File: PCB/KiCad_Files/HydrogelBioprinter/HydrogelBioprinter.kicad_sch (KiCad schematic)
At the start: 24 parts, among them J1 USB_B_Micro, J2 Conn_01x04_Pin, SW1 SW_Push, SW2 SW_SPDT, U1 STM32F407VGT6, Y1 16MHz

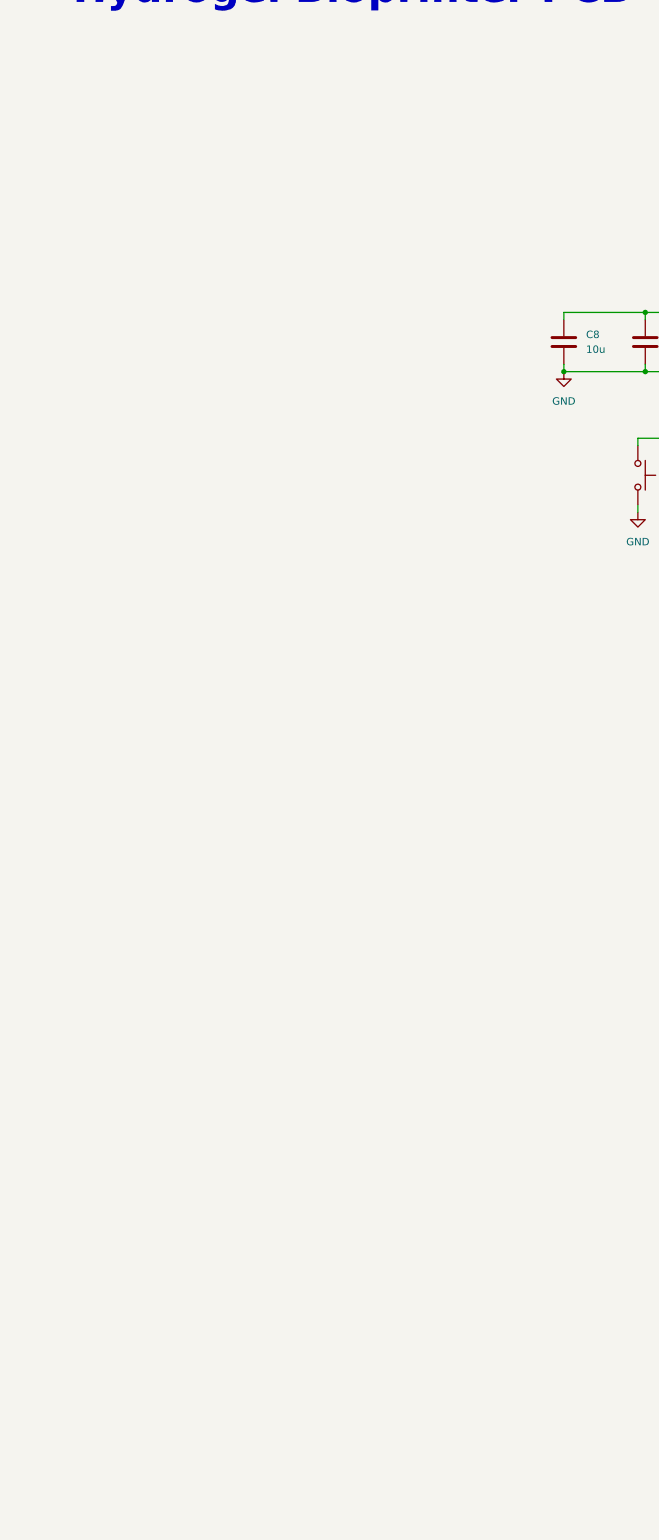
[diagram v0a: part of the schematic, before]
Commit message: Added driver connections to PCB KiCad Schematic
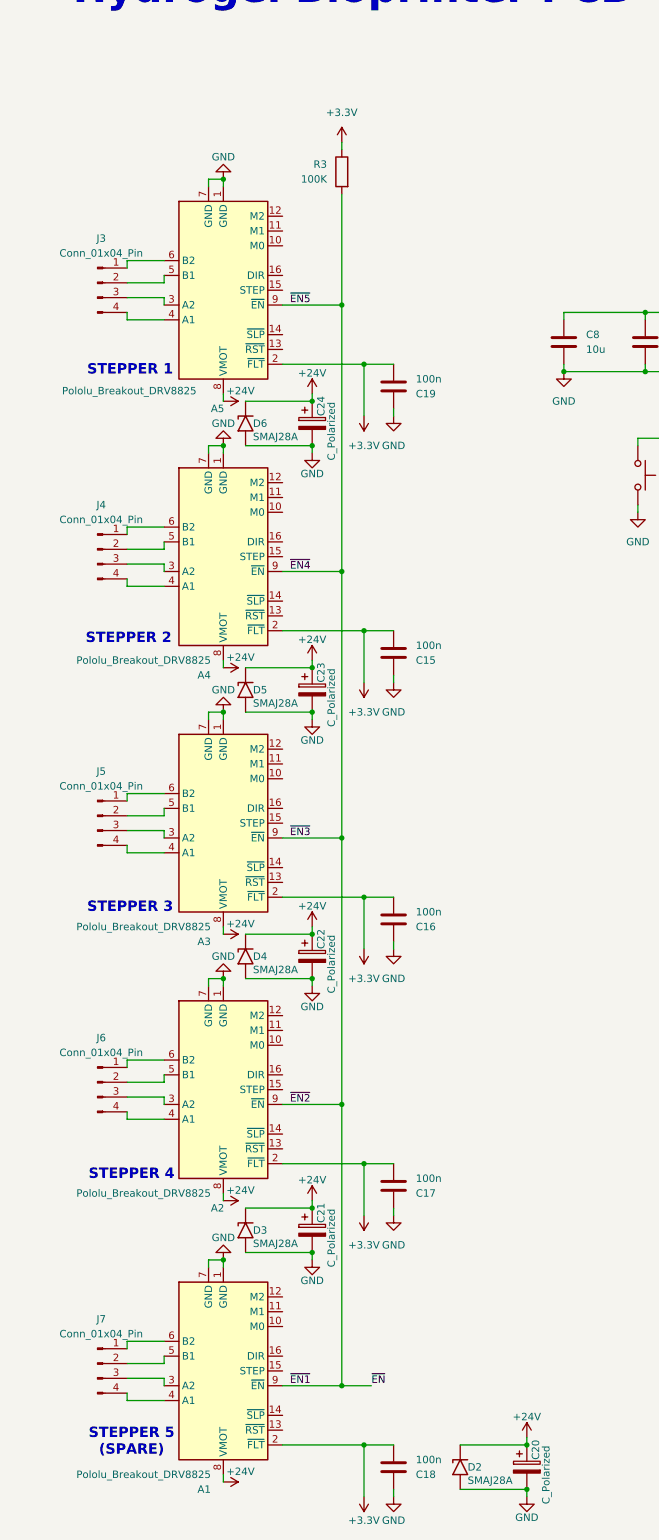
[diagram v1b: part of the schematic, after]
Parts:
- added A1, A2, A3, A4, A5: Pololu_Breakout_DRV8825, Module:Pololu_Breakout-16_15.2x20.3mm, symbol Driver_Motor:Pololu_Breakout_DRV8825
- added C15, C16, C17, C18, C19: 100n, symbol Device:C
- added C20, C21, C22, C23, C24: C_Polarized, Capacitor_SMD:CP_Elec_6.3x7.7, symbol Device:C_Polarized
- added D2, D3, D4, D5, D6: SMAJ28A, Diode_SMD:D_SMA, symbol Diode:SMAJ28A
- added J3, J4, J5, J6, J7: Conn_01x04_Pin, symbol Connector:Conn_01x04_Pin
- added R3: 100K, symbol Device:R
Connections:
- net +3.3V: now also A1.2 (~{FLT}), A2.2 (~{FLT}), A3.2 (~{FLT}), A4.2 (~{FLT}), A5.2 (~{FLT}), C15.2, C16.2, C17.2, C18.2, C19.2, R3.1
- net GND: now also A1.1 (GND), A1.7 (GND), A2.1 (GND), A2.7 (GND), A3.1 (GND), A3.7 (GND), A4.1 (GND), A4.7 (GND), A5.1 (GND), A5.7 (GND), C15.1, C16.1, C17.1, C18.1, C19.1, C20.2, C21.2, C22.2, C23.2, C24.2, D2.2 (A2), D3.2 (A2), D4.2 (A2), D5.2 (A2), D6.2 (A2)
- new net: A1.3 (A2), J7.3 (Pin_3)
- new net: A1.4 (A1), J7.4 (Pin_4)
- new net: A1.5 (B1), J7.2 (Pin_2)
- new net: A1.6 (B2), J7.1 (Pin_1)
- new net: A4.6 (B2), J4.1 (Pin_1)
- new net: A4.5 (B1), J4.2 (Pin_2)
- new net: A4.3 (A2), J4.3 (Pin_3)
- new net: A4.4 (A1), J4.4 (Pin_4)
- new net: A5.3 (A2), J3.3 (Pin_3)
- new net: A5.4 (A1), J3.4 (Pin_4)
- new net: A5.5 (B1), J3.2 (Pin_2)
- new net: A5.6 (B2), J3.1 (Pin_1)
- new net: A3.6 (B2), J5.1 (Pin_1)
- new net: A3.5 (B1), J5.2 (Pin_2)
- new net: A3.3 (A2), J5.3 (Pin_3)
- new net: A3.4 (A1), J5.4 (Pin_4)
- new net: A2.3 (A2), J6.3 (Pin_3)
- new net: A2.4 (A1), J6.4 (Pin_4)
- new net: A2.5 (B1), J6.2 (Pin_2)
- new net: A2.6 (B2), J6.1 (Pin_1)
- new net +24V: A1.8 (VMOT), A2.8 (VMOT), A3.8 (VMOT), A4.8 (VMOT), A5.8 (VMOT), C20.1, C21.1, C22.1, C23.1, C24.1, D2.1 (A1), D3.1 (A1), D4.1 (A1), D5.1 (A1), D6.1 (A1)
- new net ~{EN1}: A1.9 (~{EN}), A2.9 (~{EN}), A3.9 (~{EN}), A4.9 (~{EN}), A5.9 (~{EN}), R3.2
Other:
- note added: "STEPPER 1"
- note added: "STEPPER 2"
- note added: "STEPPER 3"
- note added: "STEPPER 4"
- note added: "STEPPER 5 (SPARE)"

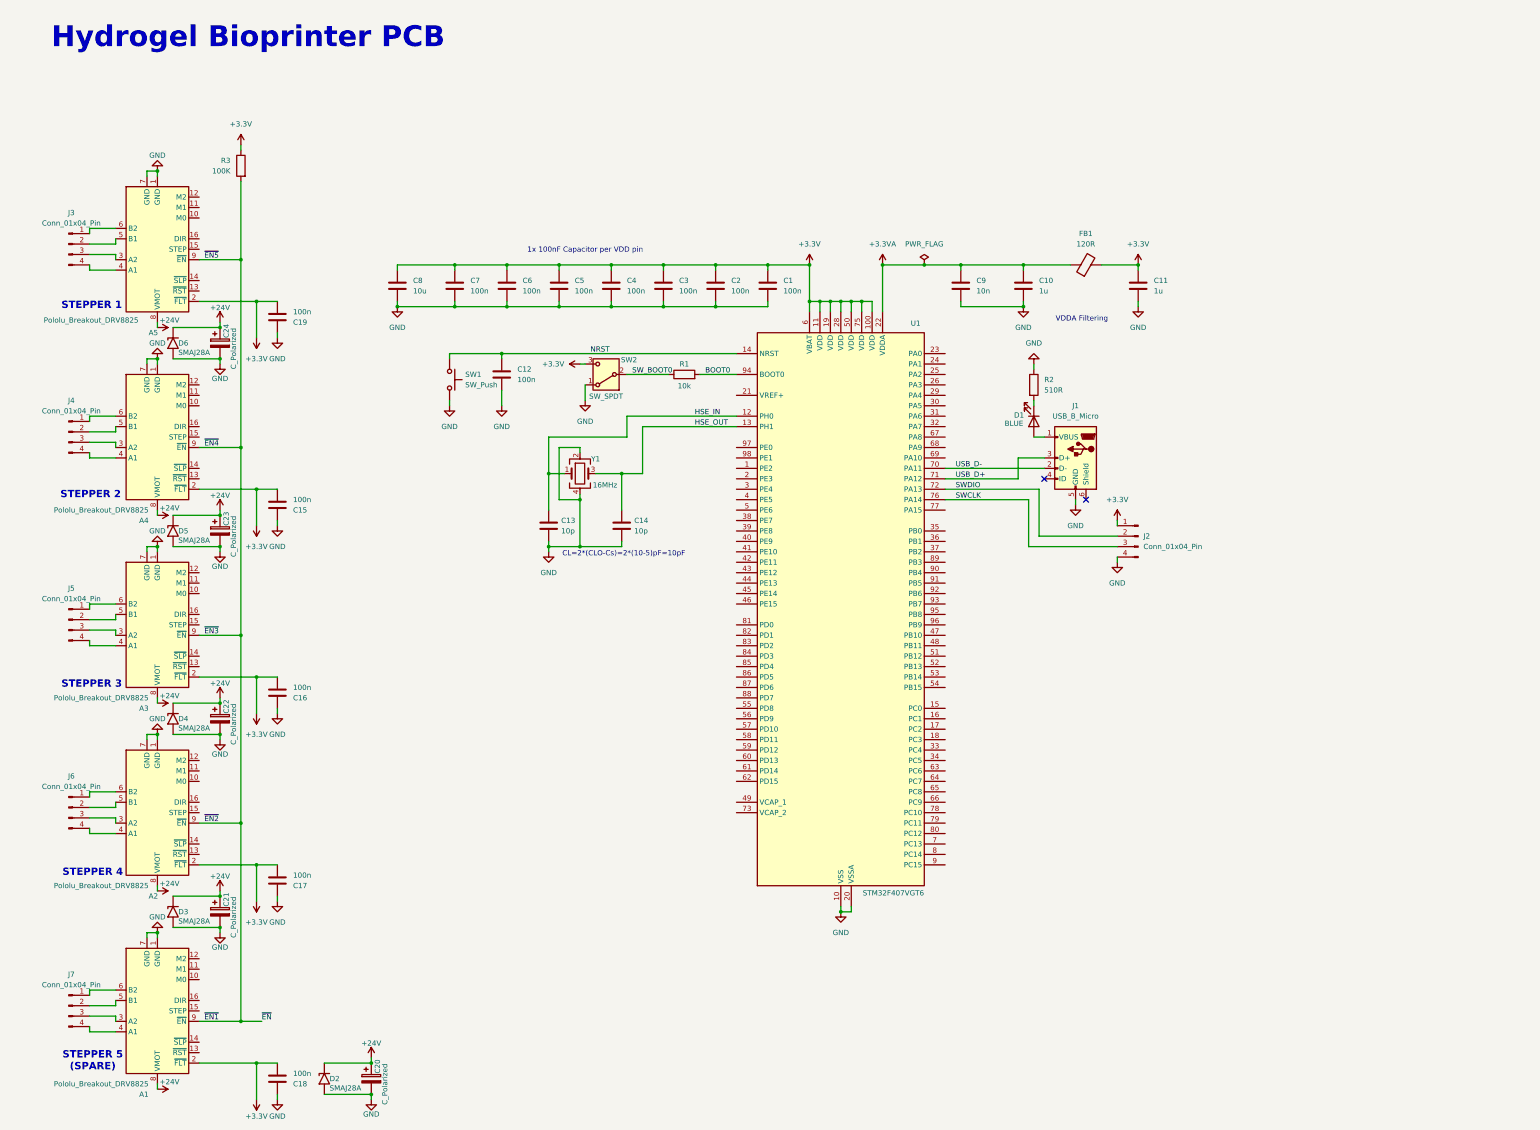
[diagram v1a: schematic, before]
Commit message: Additions to the KiCad PCB Schematic
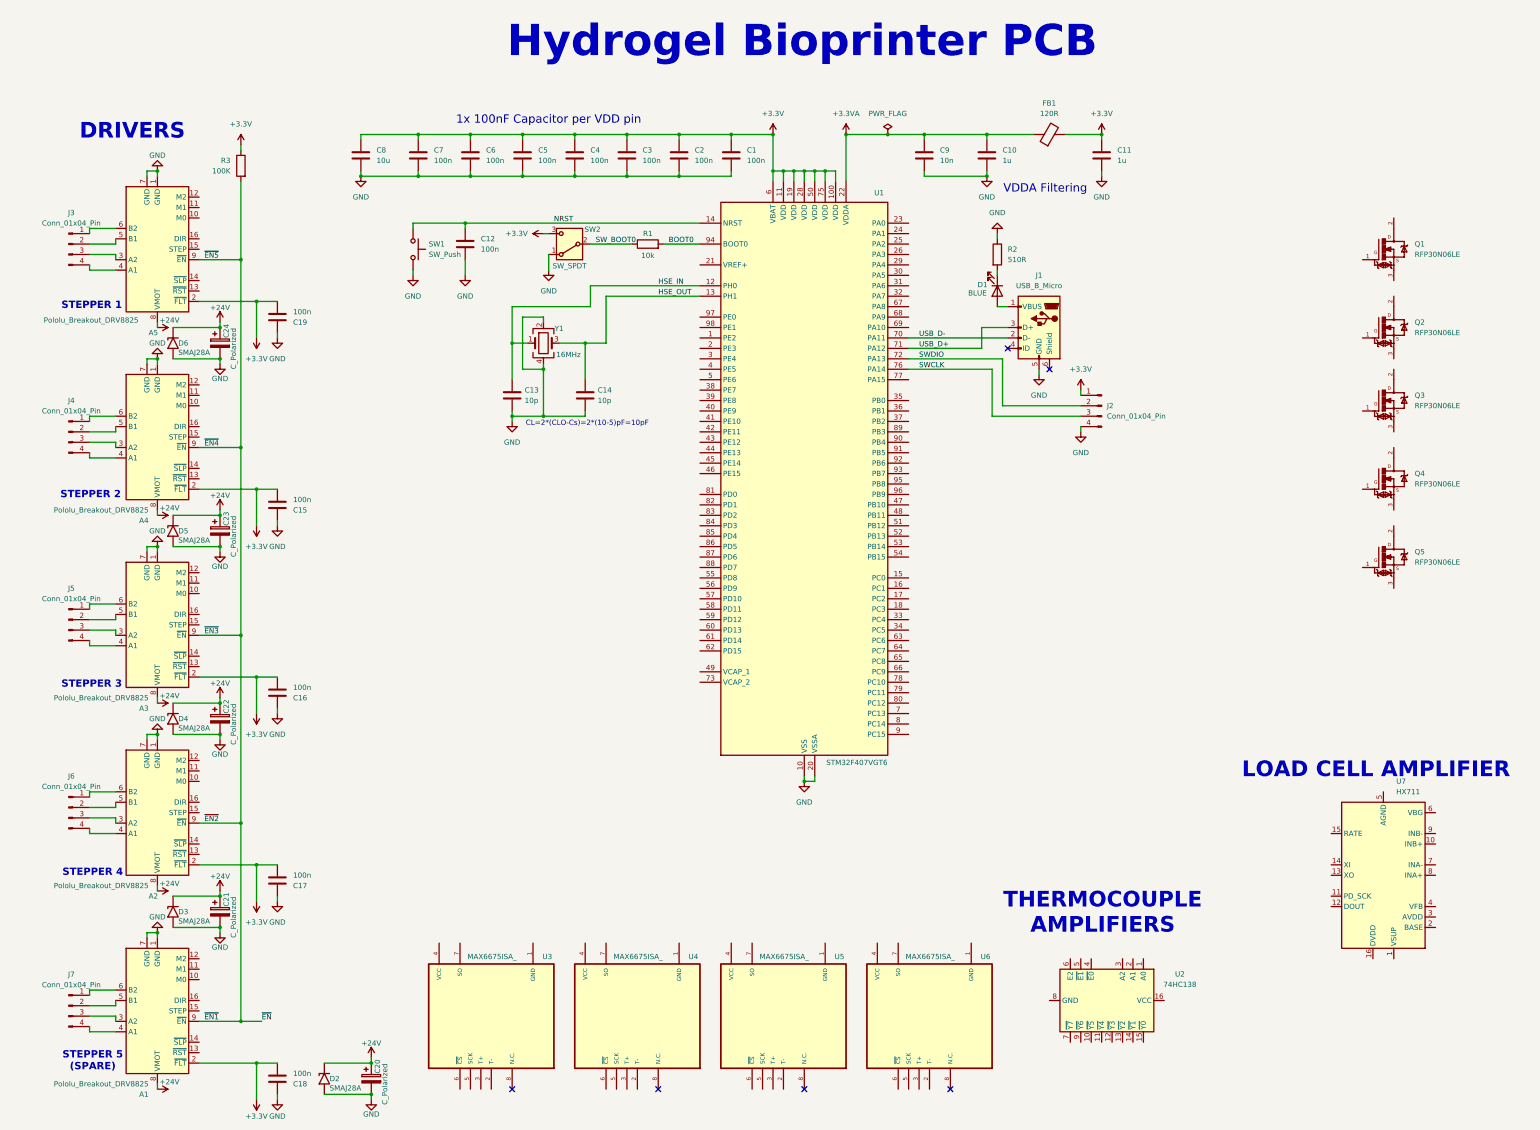
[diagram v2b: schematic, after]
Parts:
- added Q1, Q2, Q3, Q4, Q5: RFP30N06LE, RFP30N06LE:TRANS_RFP30N06LE, symbol RFP30N06LE:RFP30N06LE
- added U2: 74HC138, symbol 74xx:74HC138
- added U3, U4, U5, U6: MAX6675ISA_, MAX6675ISA_:SOIC127P600X175-8N, symbol MAX6675ISA_:MAX6675ISA_
- added U7: HX711, Package_SO:SOP-16_3.9x9.9mm_P1.27mm, symbol Analog_ADC:HX711
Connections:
- no-connect marks 2 -> 6
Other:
- note added: "DRIVERS"
- note added: "LOAD CELL AMPLIFIER"
- note added: "THERMOCOUPLE AMPLIFIERS"
- moved on the sheet: C1, C10, C11, C12, C13, C14, C2, C3, C4, C5, C6, C7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

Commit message: Finished Drivers and Thermocouple Amplifier connections in KiCad Schematic
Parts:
- added C25, C26, C27, C28, C29: 100n, symbol Device:C
- added J10, J11, J8, J9: Screw_Terminal_01x02, symbol Connector:Screw_Terminal_01x02
- A1, A2, A3, A4, A5: value Pololu_Breakout_DRV8825 -> MKS TMC2209
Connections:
- net +3.3V: now also U2.16 (VCC), U2.6 (E2), U3.4 (VCC), U4.4 (VCC), U5.4 (VCC), U6.4 (VCC), C25.2, C26.2, C27.2, C28.2, C29.2
- net GND: now also U2.4 (~{E0}), U2.5 (~{E1}), U2.8 (GND), U3.1 (GND), U4.1 (GND), U5.1 (GND), U6.1 (GND), C25.1, C26.1, C27.1, C28.1, C29.1
- net M0: now reaches A1.10 (M0)
- net M0: now also A2.10 (M0), A3.10 (M0), A4.10 (M0), A5.10 (M0)
- net M1: now reaches A1.11 (M1)
- net M1: now also A2.11 (M1), A3.11 (M1), A4.11 (M1), A5.11 (M1)
- net STEP5: now reaches A1.15 (STEP)
- net DIR5: now reaches A1.16 (DIR)
- net STEP1: now reaches A5.15 (STEP)
- net DIR1: now reaches A5.16 (DIR)
- net at U4.2 (T-): now also J9.1 (Pin_1)
- net at U4.3 (T+): now also J9.2 (Pin_2)
- net SCK: now reaches U4.5 (SCK)
- net SCK: now also U3.5 (SCK), U5.5 (SCK), U6.5 (SCK)
- net at U4.6 (~{CS}): now also U2.13 (~{Y2})
- net MISO: now reaches U4.7 (SO)
- net MISO: now also U3.7 (SO), U5.7 (SO), U6.7 (SO)
- net at U3.2 (T-): now also J8.1 (Pin_1)
- net at U3.3 (T+): now also J8.2 (Pin_2)
- net at U3.6 (~{CS}): now also U2.12 (~{Y3})
- net STEP4: now reaches A2.15 (STEP)
- net DIR4: now reaches A2.16 (DIR)
- net A0: now reaches U2.1 (A0)
- net at U2.14 (~{Y1}): now also U5.6 (~{CS})
- net at U2.15 (~{Y0}): now also U6.6 (~{CS})
- net A1: now reaches U2.2 (A1)
- net A2: now reaches U2.3 (A2)
- net STEP3: now reaches A3.15 (STEP)
- net DIR3: now reaches A3.16 (DIR)
- net at U6.2 (T-): now also J11.1 (Pin_1)
- net at U6.3 (T+): now also J11.2 (Pin_2)
- net STEP2: now reaches A4.15 (STEP)
- net DIR2: now reaches A4.16 (DIR)
- net at U5.2 (T-): now also J10.1 (Pin_1)
- net at U5.3 (T+): now also J10.2 (Pin_2)
- net ~{EN1} renamed ~{EN}
- no-connect marks 6 -> 25
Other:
- note added: "STEPPER 1 (X)"
- note added: "STEPPER 2 (Y)"
- note added: "STEPPER 3 (Z)"
- note added: "STEPPER 4 (Extruder)"
- note removed: "STEPPER 1"
- note removed: "STEPPER 2"
- note removed: "STEPPER 3"
- note removed: "STEPPER 4"
- moved on the sheet: A1, A2, A3, A4, A5, C1, C10, C11, C12, C13, C14, C15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
